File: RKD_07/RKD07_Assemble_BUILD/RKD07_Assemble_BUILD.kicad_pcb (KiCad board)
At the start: 2 copper layers, 233.4 x 200 mm, 171 parts, among them J1 Conn_01x02_Socket, J10 Conn_01x04, J11 TRRS, J12 Conn_01x06, J13 Conn_01x06, J14 Conn_01x02_Socket, J2 Conn_01x24, J3 Conn_01x24, J4 Conn_01x24, J5 Qwiic_RA, J6 Qwiic_RA, J7 Conn_01x06, J8 Conn_01x06, J9 Conn_01x04, M3 Mark, M4 Mark, M5 Mark, M6 Mark, M8 Mark, SW1 SW_Push, SW10 SW_Push, SW11 SW_Push, SW12 SW_Push, SW13 SW_Push, SW14 SW_Push, SW15 SW_Push, SW16 SW_Push, SW17 SW_Push, SW18 SW_Push, SW19 SW_Push, SW2 SW_Push, SW20 SW_Push, SW21 SW_Push, SW22 SW_Push, SW23 SW_Push, SW24 SW_Push, SW25 SW_Push, SW26 SW_Push, SW27 SW_Push, SW28 SW_Push, SW29 SW_Push, SW3 SW_Push, SW30 RotaryEncoder_Switch, SW31 SW_Push, SW4 SW_Push, SW5 SW_Push, SW51 SW_Push, SW52 SW_Push, SW53 SW_Push, SW54 SW_Push, SW55 SW_Push, SW56 SW_Push, SW57 SW_Push, SW58 SW_Push, SW59 SW_Push, SW6 SW_Push, SW60 SW_Push, SW61 SW_Push, SW62 SW_Push, SW63 SW_Push, SW64 SW_Push, SW65 SW_Push, SW66 SW_Push, SW67 SW_Push, SW68 SW_Push, SW69 SW_Push, SW7 SW_Push, SW70 SW_Push, SW71 SW_Push, SW72 SW_Push, SW73 SW_Push, SW74 SW_Push, SW75 SW_Push, SW76 SW_Push, SW77 SW_Push, SW78 SW_Push, SW79 SW_Push, SW8 SW_Push, SW80 SW_Push, SW81 SW_Push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

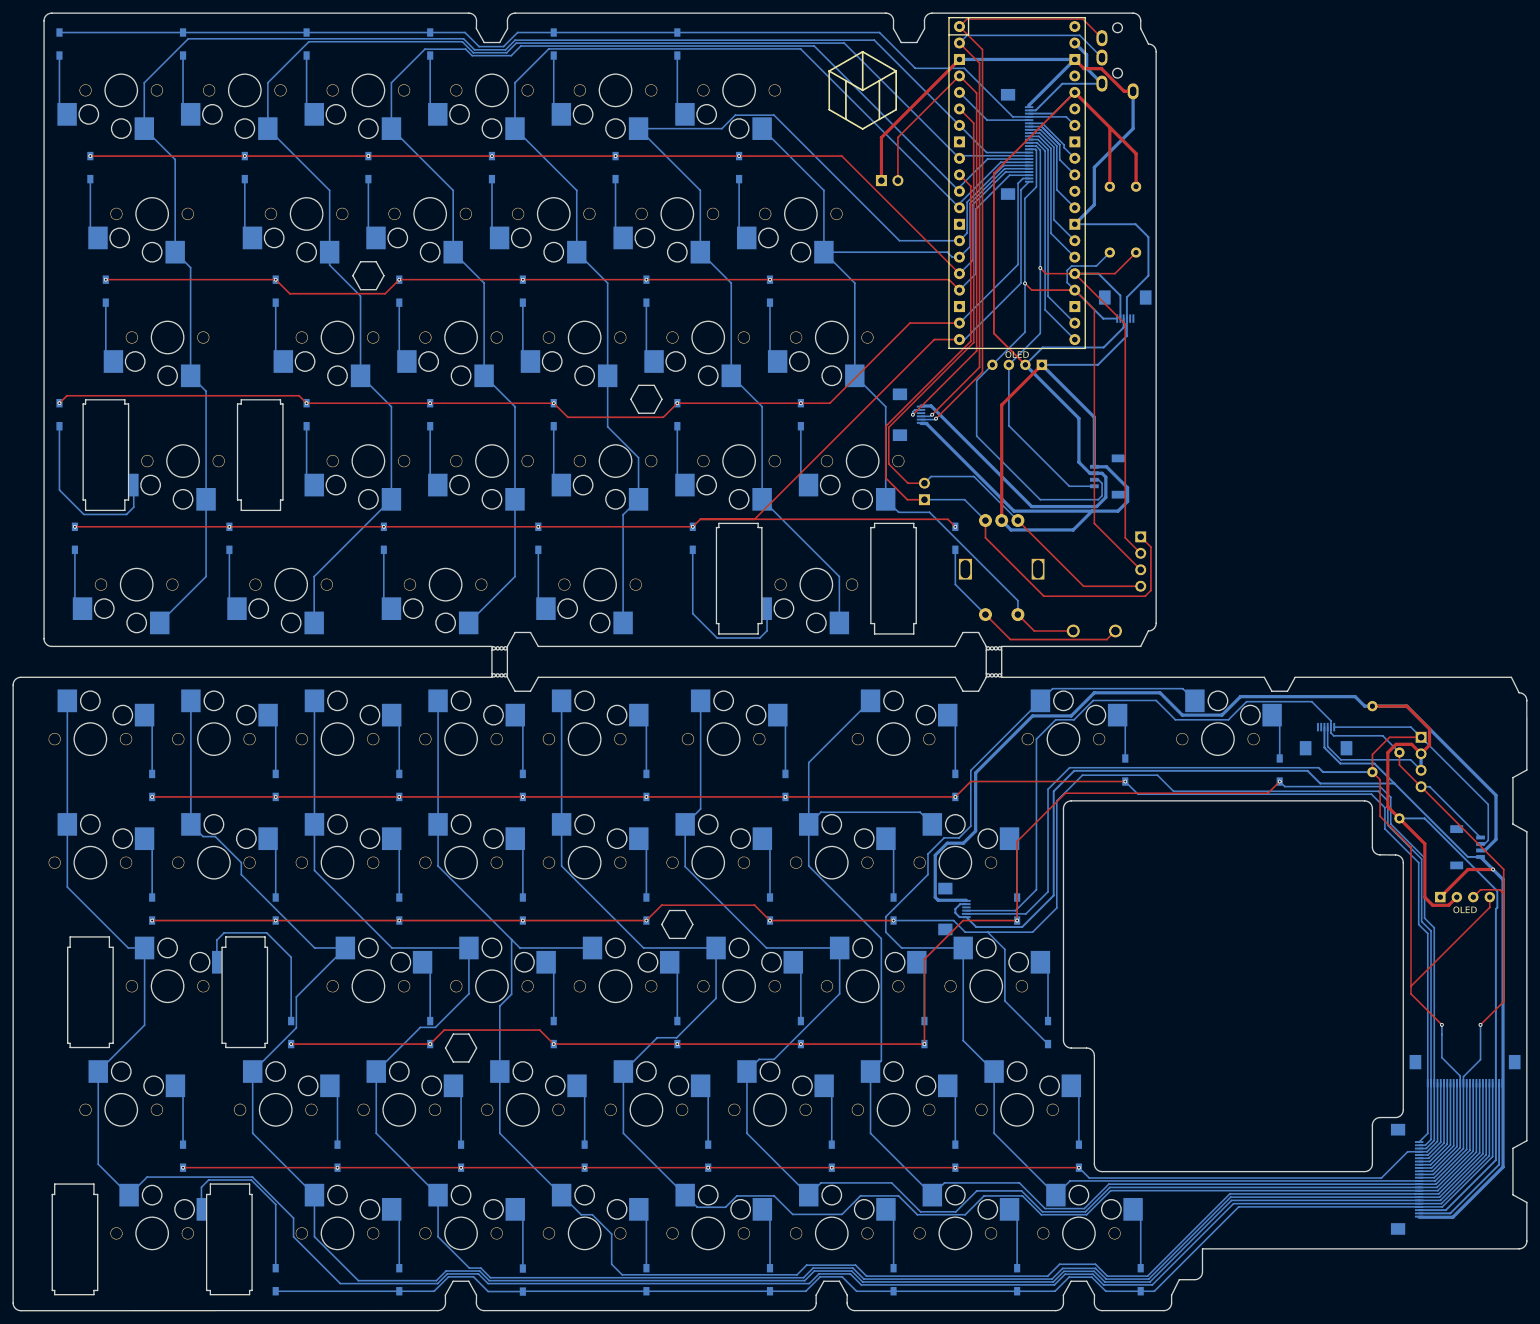
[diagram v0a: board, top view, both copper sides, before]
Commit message: 上幅を調整
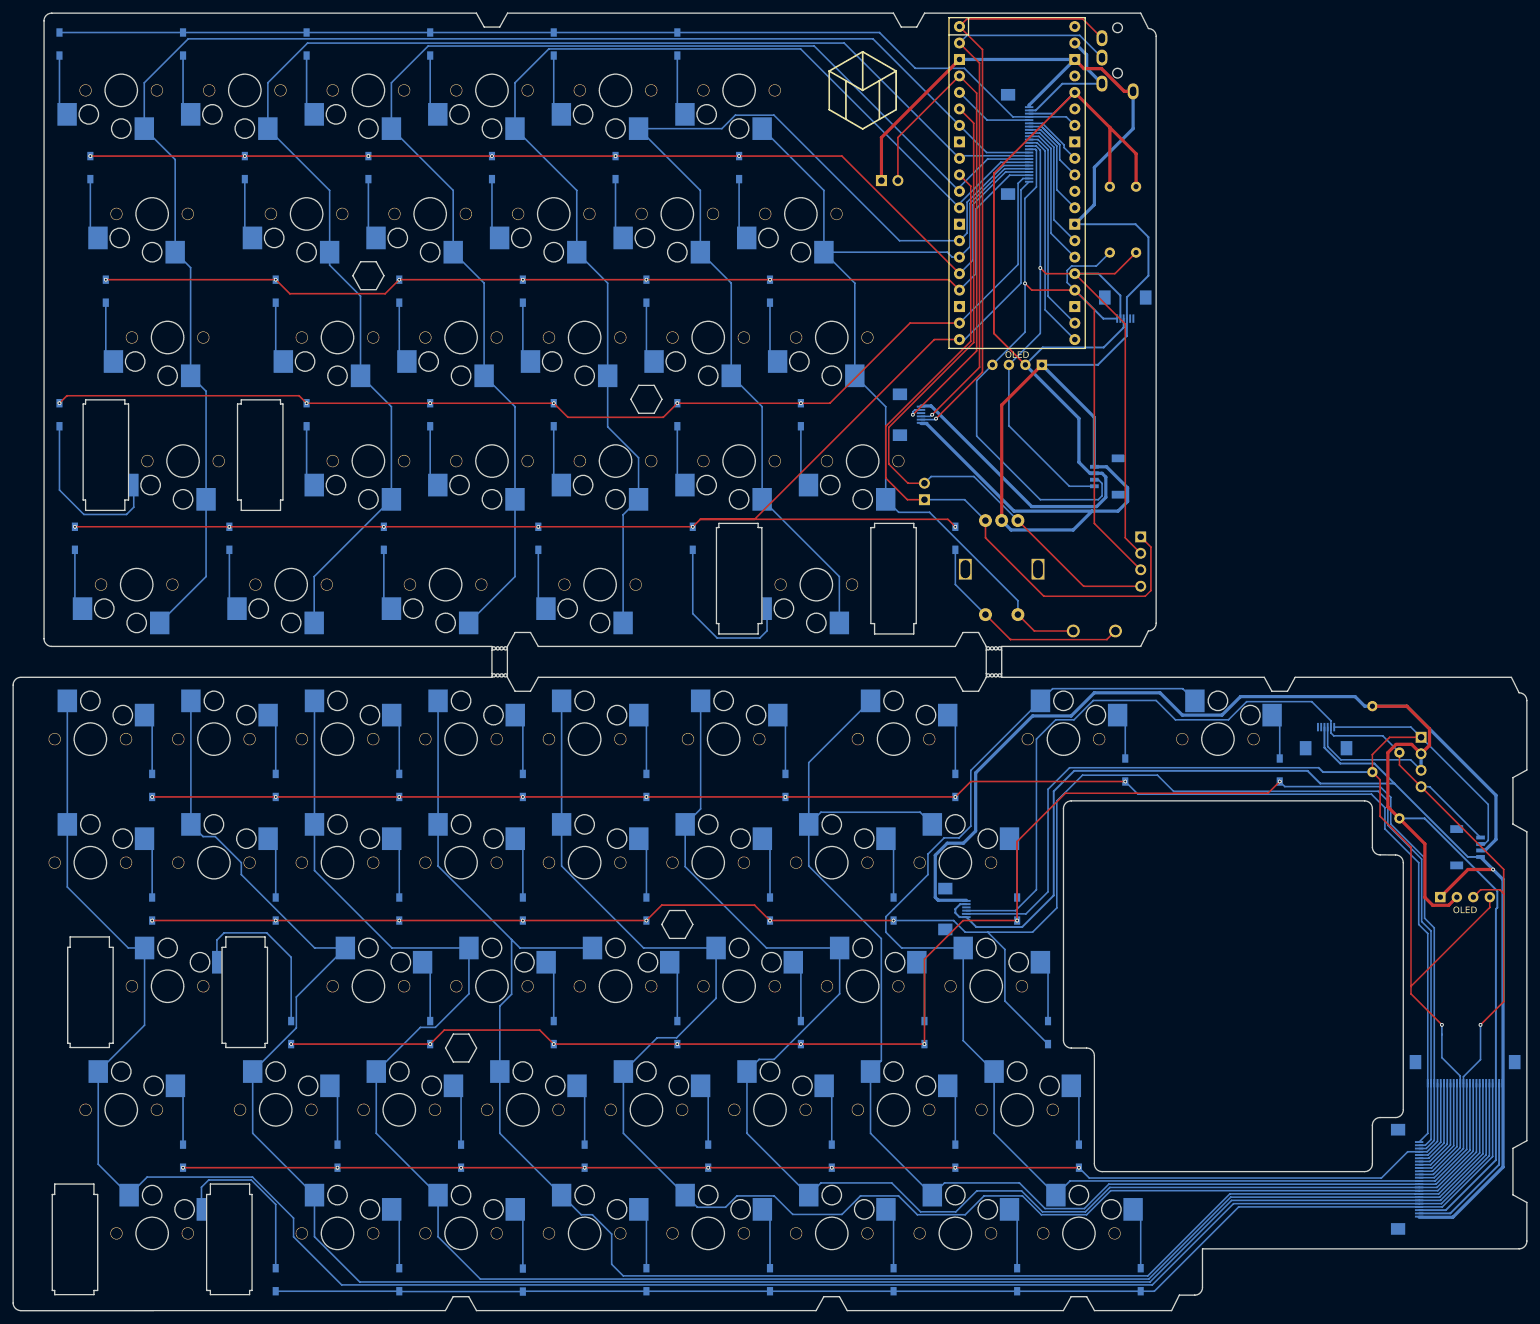
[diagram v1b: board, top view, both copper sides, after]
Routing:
- net ROW0_R: track 213.0 -> 207.6 mm
- net COL13_R: track 330.2 -> 326.4 mm
- net COL12_R: track 314.4 -> 310.6 mm
- net COL10_R: track 268.9 -> 266.1 mm
- net COL11_R: track 295.9 -> 293.3 mm
- net ROW0_L: track 164.3 -> 162.5 mm
- net COL1_L: track 225.1 -> 223.7 mm
- net COL0_L: track 237.9 -> 236.7 mm
- net COL2_L: track 207.3 -> 206.5 mm
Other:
- outline, holes or cut-outs redrawn

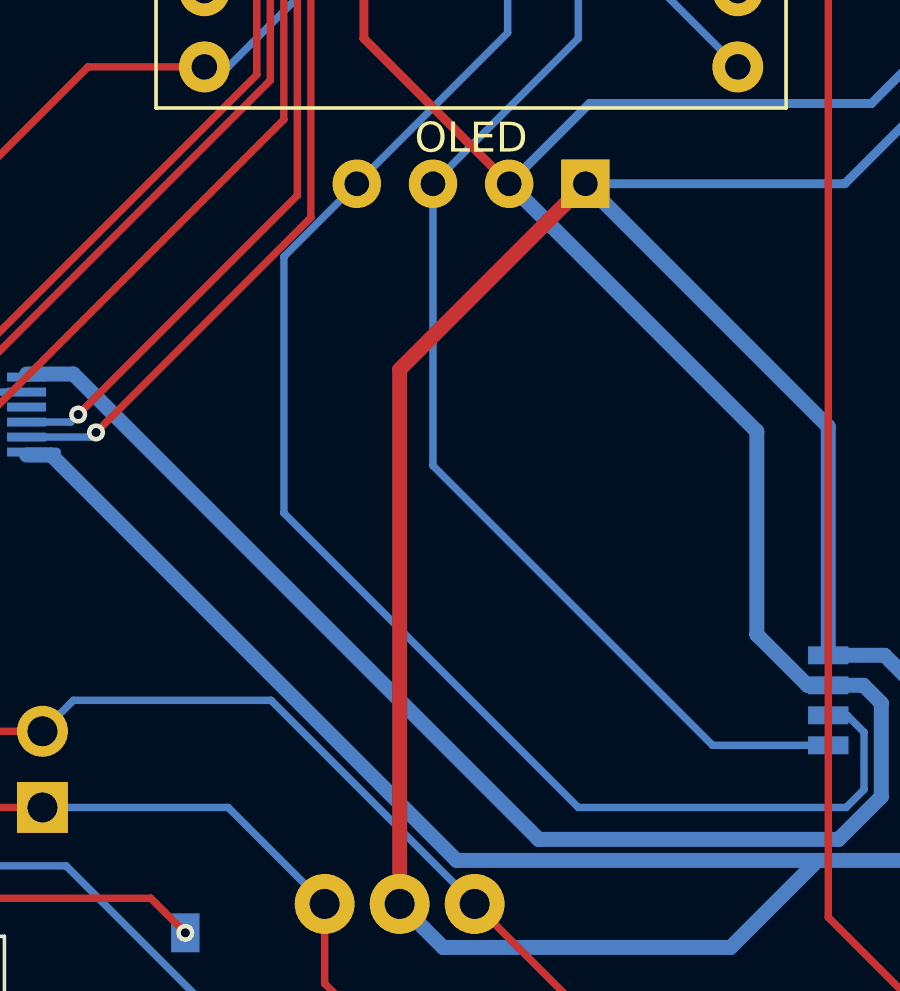
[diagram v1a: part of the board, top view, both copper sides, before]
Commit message: RePicotに伴う修正
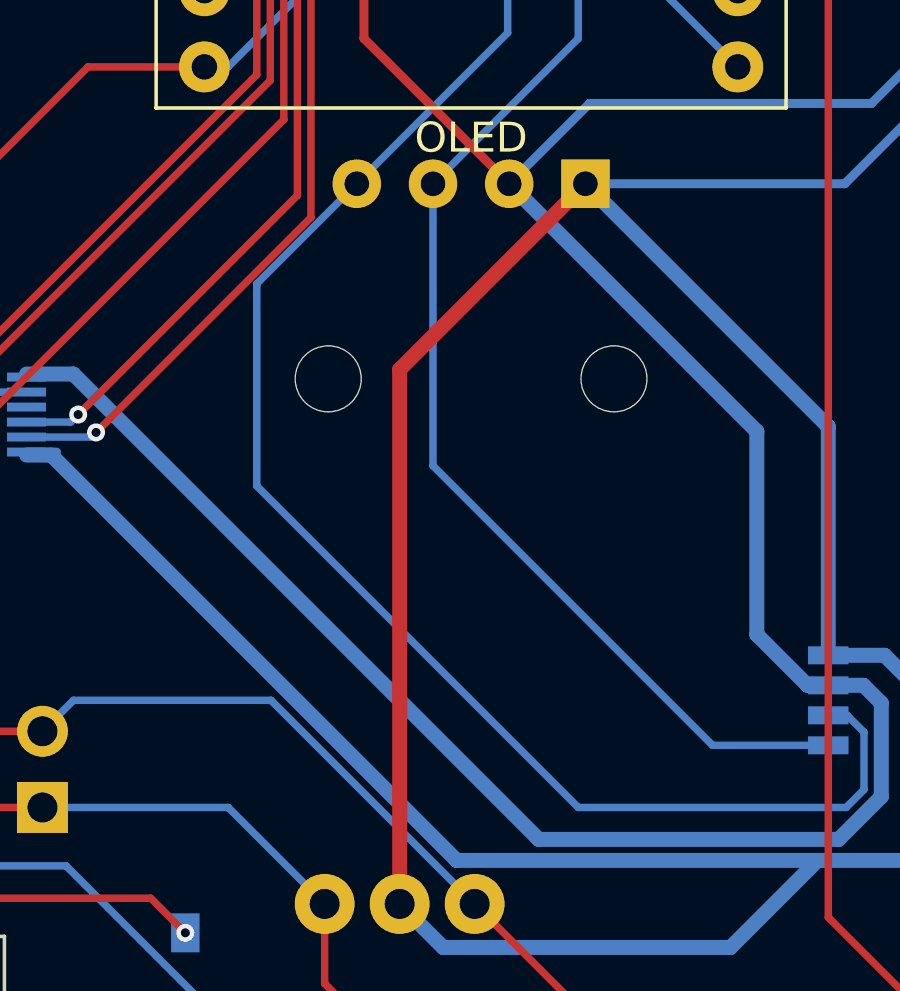
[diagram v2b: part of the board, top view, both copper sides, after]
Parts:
- added Point1: Guard_Screw_Hall, Rikkodo_FootPrint:rkd_Guard_Screw_Hall, F.Cu at (173.8, 52.4)
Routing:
- net SDA/SCK_L: track 151.1 -> 151.8 mm
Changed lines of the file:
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@@
 		)
 	)
+	(footprint "Rikkodo_FootPrint:rkd_Guard_Screw_Hall"
+		(layer "F.Cu")
+		(at 173.83125 52.3875 -90)
+		(property "Reference" "Point1"
+			(at 7 8.1 90)
+			(layer "F.SilkS")
+			(hide yes)
+			(effects
+				(font
+					(size 1 1)
+					(thickness 0.15)
+				)
+			)
+		)
+		(property "Value" "Guard_Screw_Hall"
+			(at -7.4 -8.1 90)
+			(layer "F.Fab")
+			(hide yes)
+			(effects
+				(font
+					(size 1 1)
+					(thickness 0.15)
+				)
+			)
+		)
+		(property "Datasheet" ""
+			(at 0 0 90)
+			(layer "F.Fab")
+			(hide yes)
+			(effects
+				(font
+					(size 1.27 1.27)
+					(thickness 0.15)
+				)
+			)
+		)
+		(property "Description" ""
+			(at 0 0 90)
+			(layer "F.Fab")
+			(hide yes)
+			(effects
+				(font
+					(size 1.27 1.27)
+					(thickness 0.15)
+				)
+			)
+		)
+		(attr through_hole board_only exclude_from_pos_files)
+		(fp_circle
+			(center 29.765625 4.7625)
+			(end 31.965625 4.7625)
+			(stroke
+				(width 0.15)
+				(type solid)
+			)
+			(fill no)
+			(layer "Cmts.User")
+		)
+		(fp_circle
+			(center 29.765625 -4.7625)
+			(end 31.965625 -4.7625)
+			(stroke
+				(width 0.15)
+				(type solid)
+			)
+			(fill no)
+			(layer "Cmts.User")
+		)
+		(fp_circle
+			(center 29.765625 4.7625)
+			(end 32.215625 4.7625)
+			(stroke
+				(width 0.05)
+				(type solid)
+			)
+			(fill no)
+			(layer "F.CrtYd")
+		)
+		(fp_circle
+			(center 29.765625 -4.7625)
+			(end 32.215625 -4.7625)
+			(stroke
+				(width 0.05)
+				(type solid)
+			)
+			(fill no)
+			(layer "F.CrtYd")
+		)
+		(fp_rect
+			(start -32.146875 -11.90625)
+			(end 32.146875 11.90625)
+			(stroke
+				(width 0.1)
+				(type default)
+			)
+			(fill no)
+			(layer "F.Fab")
+		)
+		(pad "" np_thru_hole circle
+			(at 29.765625 -4.7625 270)
+			(size 2.2 2.2)
+			(drill 2.2)
+			(layers "*.Cu" "*.Mask")
+		)
+		(pad "" np_thru_hole circle
+			(at 29.765625 4.7625 270)
+			(size 2.2 2.2)
+			(drill 2.2)
+			(layers "*.Cu" "*.Mask")
+		)
+		(embedded_fonts no)
+	)
 	(footprint "Rikkodo_FootPrint:rkd_Asm_ChocV1V2_Hotswap_1u"
 		(layer "F.Cu")
@@
 	)
 	(segment
-		(start 186.3645 93.36875)
-		(end 185.7375 93.36875)
+		(start 186.332953 96.440766)
+		(end 186.928266 95.845453)
 		(width 0.25)
 		(layer "B.Cu")
@@
 	)
 	(segment
-		(start 167.59275 78.0785)
-		(end 167.59275 86.630258)
+		(start 189.25 68.525)
+		(end 187.11125 68.525)
+		(width 0.3)
+		(layer "B.Cu")
+		(net 60)
+	)
+	(segment
+		(start 177.403258 96.440766)
+		(end 186.332953 96.440766)
 		(width 0.25)
 		(layer "B.Cu")
@@
 	)
 	(segment
-		(start 186.928266 95.845453)
-		(end 186.928266 93.932516)
+		(start 175.022006 63.103125)
+		(end 175.022006 50.006352)
 		(width 0.25)
 		(layer "B.Cu")
@@
 	)
 	(segment
-		(start 189.25 68.525)
-		(end 187.11125 68.525)
-		(width 0.3)
+		(start 186.3645 93.36875)
+		(end 185.7375 93.36875)
+		(width 0.25)
 		(layer "B.Cu")
 		(net 60)
 	)
 	(segment
-		(start 175.022006 63.103125)
-		(end 175.022006 50.006352)
+		(start 166.6875 85.725008)
+		(end 177.403258 96.440766)
 		(width 0.25)
 		(layer "B.Cu")
@@
 	)
 	(segment
-		(start 167.59275 86.630258)
-		(end 177.403258 96.440766)
+		(start 166.6875 78.98375)
+		(end 166.6875 85.725008)
 		(width 0.25)
 		(layer "B.Cu")
@@
 	)
 	(segment
+		(start 186.928266 93.932516)
+		(end 186.3645 93.36875)
+		(width 0.25)
+		(layer "B.Cu")
+		(net 60)
+	)
+	(segment
+		(start 186.928266 95.845453)
+		(end 186.928266 93.932516)
+		(width 0.25)
+		(layer "B.Cu")
+		(net 60)
+	)
+	(segment
 		(start 175.050106 63.105141)
 		(end 175.024022 63.105141)
@@
 	)
 	(segment
-		(start 177.403258 96.440766)
-		(end 186.332953 96.440766)
-		(width 0.25)
-		(layer "B.Cu")
-		(net 60)
-	)
-	(segment
 		(start 181.54525 61.107884)
 		(end 181.54525 62.959)
@@
 	)
 	(segment
-		(start 186.928266 93.932516)
-		(end 186.3645 93.36875)
+		(start 170.02125 75.65)
+		(end 166.6875 78.98375)
 		(width 0.25)
 		(layer "B.Cu")
@@
 	)
 	(segment
-		(start 186.332953 96.440766)
-		(end 186.928266 95.845453)
-		(width 0.25)
-		(layer "B.Cu")
-		(net 60)
-	)
-	(segment
 		(start 182.234134 60.419)
 		(end 181.54525 61.107884)
 		(width 0.25)
 		(layer "B.Cu")
-		(net 60)
-	)
-	(segment
-		(start 170.02125 75.65)
-		(end 167.59275 78.0785)
-		(width 0.25)
-		(layer "B.Cu")

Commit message: 07 Release調整
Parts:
- SW25, SW4, SW86, SW88: footprint Rikkodo_FootPrint:rkd_Asm_ChocV2_Hotswap_2uW -> Rikkodo_FootPrint:rkd_Asm_ChocV2_Hotswap_2u

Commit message: CSをGND固定
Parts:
- removed J14: Conn_01x02_Socket, Connector_PinHeader_2.54mm:PinHeader_1x02_P2.54mm_Horizontal
- added OL1: OLED, kicad:AZ1UBALL, B.Cu at (150.0, 33.3)
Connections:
- J8 pad 5: CS/GND -> GND_L
- U1 pad 4: CS/GND -> GND_L
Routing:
- net CS/GND: track 80.2 -> 0.00 mm, vias 1 -> 0
- net 3v3_L: track 166.2 -> 217.9 mm
- net SDA/SCK_L: track 151.8 -> 192.6 mm
- net SCL/TX_L: track 139.8 -> 175.9 mm
- net GND_L: track 240.2 -> 247.9 mm
- net UART_TX/SCK_L: track 91.2 -> 91.8 mm
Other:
- board text added: "SDA SCL VCC GND"
- board text removed: "CS/HandDetect"
- board text removed: "GND"

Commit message: I2Cを色々追加
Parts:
- added J14: Conn_01x04, Connector_PinSocket_2.54mm:PinSocket_1x04_P2.54mm_Vertical, B.Cu at (239.1, 164.3)
- added J15: Conn_01x04, Connector_PinSocket_2.54mm:PinSocket_1x04_P2.54mm_Vertical, B.Cu at (239.1, 160.7)
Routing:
- net 3v3_R: track 281.9 -> 288.6 mm
- net SCL/TX_R: track 197.3 -> 203.9 mm
- net GND_R: track 201.1 -> 207.7 mm
- net SDA/SCK_R: track 218.8 -> 220.6 mm
- net COL10_R: track 266.1 -> 266.7 mm
